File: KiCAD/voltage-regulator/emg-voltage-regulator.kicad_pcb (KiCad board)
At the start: 2 copper layers, 30 x 50 mm, 15 parts, among them J1 Conn_01x03_Male, U1 MAX764ESA+

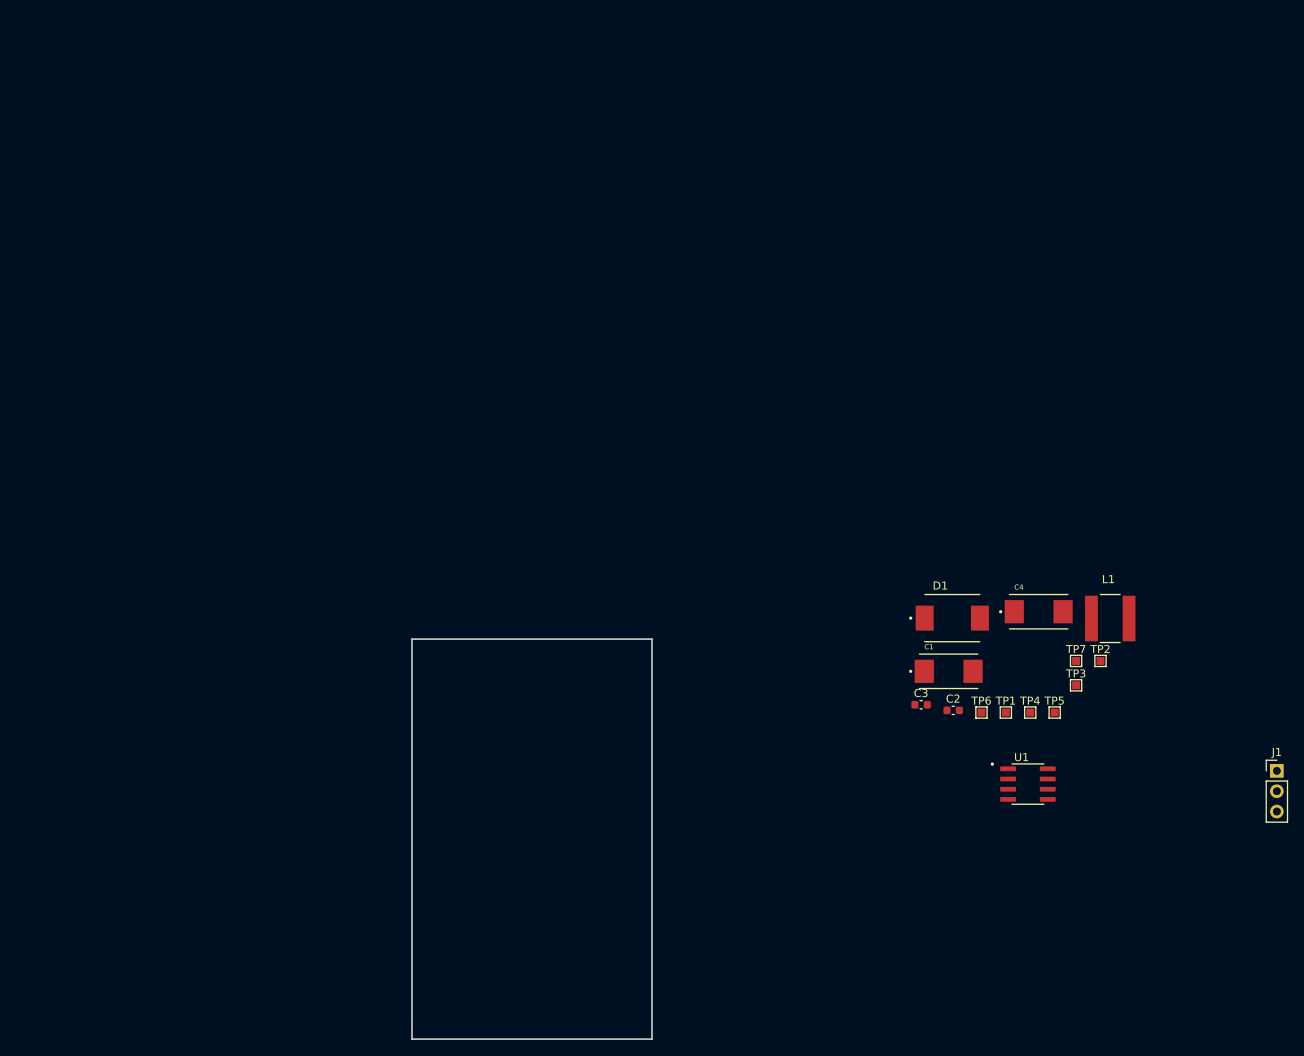
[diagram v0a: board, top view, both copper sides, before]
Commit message: layout for voltage regulator done
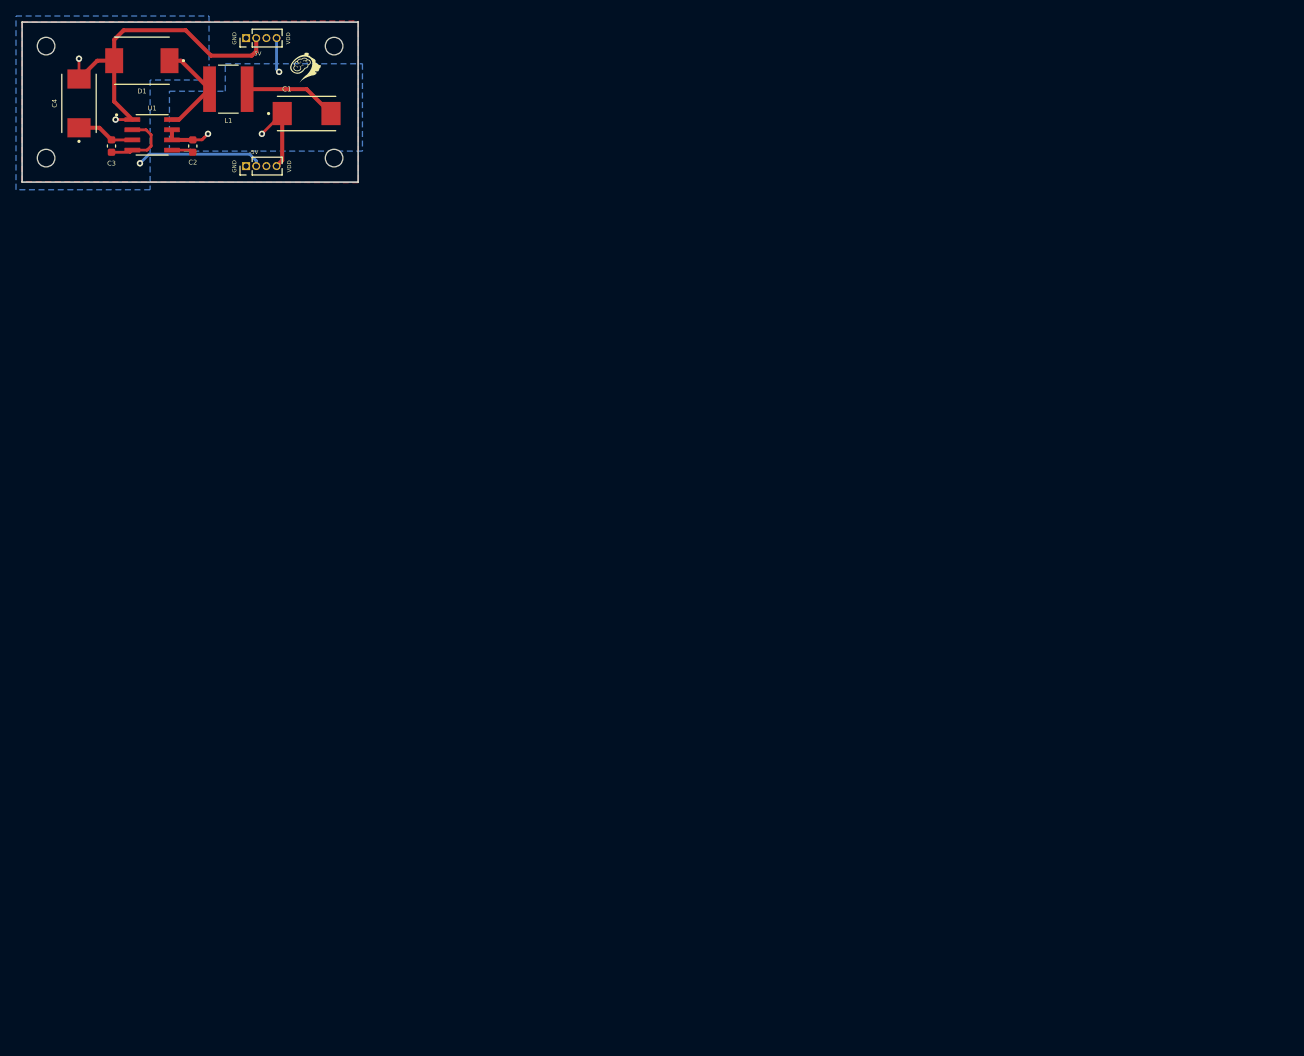
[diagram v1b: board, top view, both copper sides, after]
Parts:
- removed TP1, TP2, TP3, TP4, TP5, TP6, TP7: TestPoint, TestPoint:TestPoint_Pad_1.0x1.0mm
- added G***: LOGO, LOGO, F.Cu at (35.4, 5.71)
- added H1: MountingHole, MountingHole:MountingHole_2.2mm_M2, F.Cu at (3.00, 17.0)
- added H2: MountingHole, MountingHole:MountingHole_2.2mm_M2, F.Cu at (39.0, 17.0)
- added H3: MountingHole, MountingHole:MountingHole_2.2mm_M2, F.Cu at (3.00, 3.00)
- added H4: MountingHole, MountingHole:MountingHole_2.2mm_M2, F.Cu at (39.0, 3.00)
- added J2: Conn_01x04_Female, Connector_PinHeader_1.27mm:PinHeader_1x04_P1.27mm_Vertical, F.Cu at (28.0, 2.00)
- J1: value Conn_01x03_Male -> Conn_01x04_Female; footprint Connector_PinHeader_2.54mm:PinHeader_1x03_P2.54mm_Vertical -> Connector_PinHeader_1.27mm:PinHeader_1x04_P1.27mm_Vertical
- moved J1 149.4 mm to (28.0, 18.0), turned to 90 degrees
- moved U1 136.3 mm to (16.3, 14.1)
- moved C4 135.8 mm to (7.11, 10.2), turned to 90 degrees
- moved L1 128.6 mm to (25.8, 8.38)
- moved C3 123.0 mm to (11.2, 15.5), turned to 90 degrees
- moved D1 123.0 mm to (15.0, 4.83), turned to 180 degrees
- moved C2 118.4 mm to (21.3, 15.5), turned to -90 degrees
- moved C1 106.3 mm to (35.6, 11.4)
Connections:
- J1 pad 1: VDD -> GND
- J1 pad 2: unconnected-(J1-Pad2) -> -5V
- J1 pad 3: GND -> unconnected-(J1-Pad3)
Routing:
- net -5V: track 0.00 -> 58.4 mm, vias 0 -> 3
- net GND: track 0.00 -> 21.8 mm
- net VDD: track 0.00 -> 20.9 mm, vias 0 -> 3
- net /LX: track 0.00 -> 12.8 mm
- net /FB/REF: track 0.00 -> 9.28 mm
- added copper zone on B.Cu, net -5V
- added copper zone on F.Cu, net GND
- added copper zone on B.Cu, net VDD
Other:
- board size 30 x 50 mm -> 42 x 20 mm
- board text added: "-5V"
- board text added: "GND"
- board text added: "VDD"

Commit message: added VSS input to the AFE board
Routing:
- net VDD: track 20.9 -> 29.3 mm, vias 3 -> 2
- net -5V: track 58.4 -> 62.7 mm, vias 3 -> 2
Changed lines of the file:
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@@
   )
   (gr_text "-5V" (at 28.956 16.256) (layer "F.SilkS")
-    (effects (font (size 0.5 0.5) (thickness 0.125)))
+    (effects (font (size 0.5 0.4) (thickness 0.1)))
   )
-  (gr_text "-5V" (at 29.337 3.937) (layer "F.SilkS")
-    (effects (font (size 0.5 0.5) (thickness 0.125)))
+  (gr_text "-5V" (at 29.21 3.937) (layer "F.SilkS")
+    (effects (font (size 0.5 0.4) (thickness 0.1)))
   )
   (gr_text "VDD\n" (at 33.401 18.034 90) (layer "F.SilkS")
@@
   (segment (start 29.972 13.968) (end 32.51 11.43) (width 0.3556) (layer "F.Cu") (net 1))
   (segment (start 22.492 14.719) (end 22.733 14.478) (width 0.3556) (layer "F.Cu") (net 1))
-  (via blind (at 32.131 6.223) (size 0.8) (drill 0.4) (layers "F.Cu" "B.Cu") (net 1))
   (via blind (at 23.241 13.97) (size 0.8) (drill 0.4) (layers "F.Cu" "B.Cu") (net 1))
   (via blind (at 29.972 13.97) (size 0.8) (drill 0.4) (layers "F.Cu" "B.Cu") (net 1))
-  (segment (start 31.81 5.902) (end 32.131 6.223) (width 0.3556) (layer "B.Cu") (net 1))
-  (segment (start 31.81 2) (end 31.81 5.902) (width 0.3556) (layer "B.Cu") (net 1))
+  (segment (start 31.81 2) (end 31.81 12.132) (width 0.3556) (layer "B.Cu") (net 1))
+  (segment (start 31.81 12.132) (end 29.972 13.97) (width 0.3556) (layer "B.Cu") (net 1))
   (segment (start 21.069 16.002) (end 21.336 16.269) (width 0.3556) (layer "F.Cu") (net 2))
   (segment (start 9.667 13.21) (end 11.176 14.719) (width 0.508) (layer "F.Cu") (net 2))
@@
   (via blind (at 7.112 4.572) (size 0.8) (drill 0.4) (layers "F.Cu" "B.Cu") (net 4))
   (via blind (at 11.684 12.192) (size 0.8) (drill 0.4) (layers "F.Cu" "B.Cu") (net 4))
-  (via blind (at 14.732 17.653) (size 0.8) (drill 0.4) (layers "F.Cu" "B.Cu") (net 4))
-  (segment (start 28.448 16.51) (end 15.875 16.51) (width 0.3556) (layer "B.Cu") (net 4))
-  (segment (start 15.875 16.51) (end 14.732 17.653) (width 0.3556) (layer "B.Cu") (net 4))
-  (segment (start 29.27 17.332) (end 29.27 18) (width 0.3556) (layer "B.Cu") (net 4))
-  (segment (start 28.448 16.51) (end 29.27 17.332) (width 0.3556) (layer "B.Cu") (net 4))
+  (segment (start 29.27 18) (end 29.27 17.332) (width 0.3556) (layer "B.Cu") (net 4))
+  (segment (start 29.27 17.332) (end 28.448 16.51) (width 0.3556) (layer "B.Cu") (net 4))
+  (segment (start 16.002 16.51) (end 11.684 12.192) (width 0.3556) (layer "B.Cu") (net 4))
+  (segment (start 28.448 16.51) (end 16.002 16.51) (width 0.3556) (layer "B.Cu") (net 4))
   (segment (start 19.875 4.826) (end 23.431 8.382) (width 0.508) (layer "F.Cu") (net 5))
   (segment (start 19.621 12.192) (end 23.431 8.382) (width 0.508) (layer "F.Cu") (net 5))
